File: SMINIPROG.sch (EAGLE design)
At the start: 5 parts

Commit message: Routing for v1.0 release
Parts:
- added J1: ESPROG-SOCKET, SuperHouse-Connectors:ESPROG-SOCKET
- added J2: M01-PLAIN, SuperHouse-Connectors:M01-PLAIN
- added TP6, TP7: POGO-P75-B1, SuperHouse-Test:POGO-P75-B1
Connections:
- new net !RESET: J1.6, TP7.P$1
- new net 3.3V: J1.3, TP1.P$1
- new net GPIO0: J1.2, TP5.P$1
- new net GPIO2: J2.1, TP6.P$1
- new net SONOFF_RX: J1.4, TP4.P$1
- new net SONOFF_TX: J1.5, TP3.P$1
- net GND: now also J1.1
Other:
- note added: "!RESET"
- note added: "GPIO2"
- note removed: "TX and RX connected directly to programmer. Pull 3.3V and GPIO0 low. Raise 3.3V. Hold GPIO0 low for a while, then raise or release."
- moved on the sheet: TP1, TP2, TP3, TP4, TP5

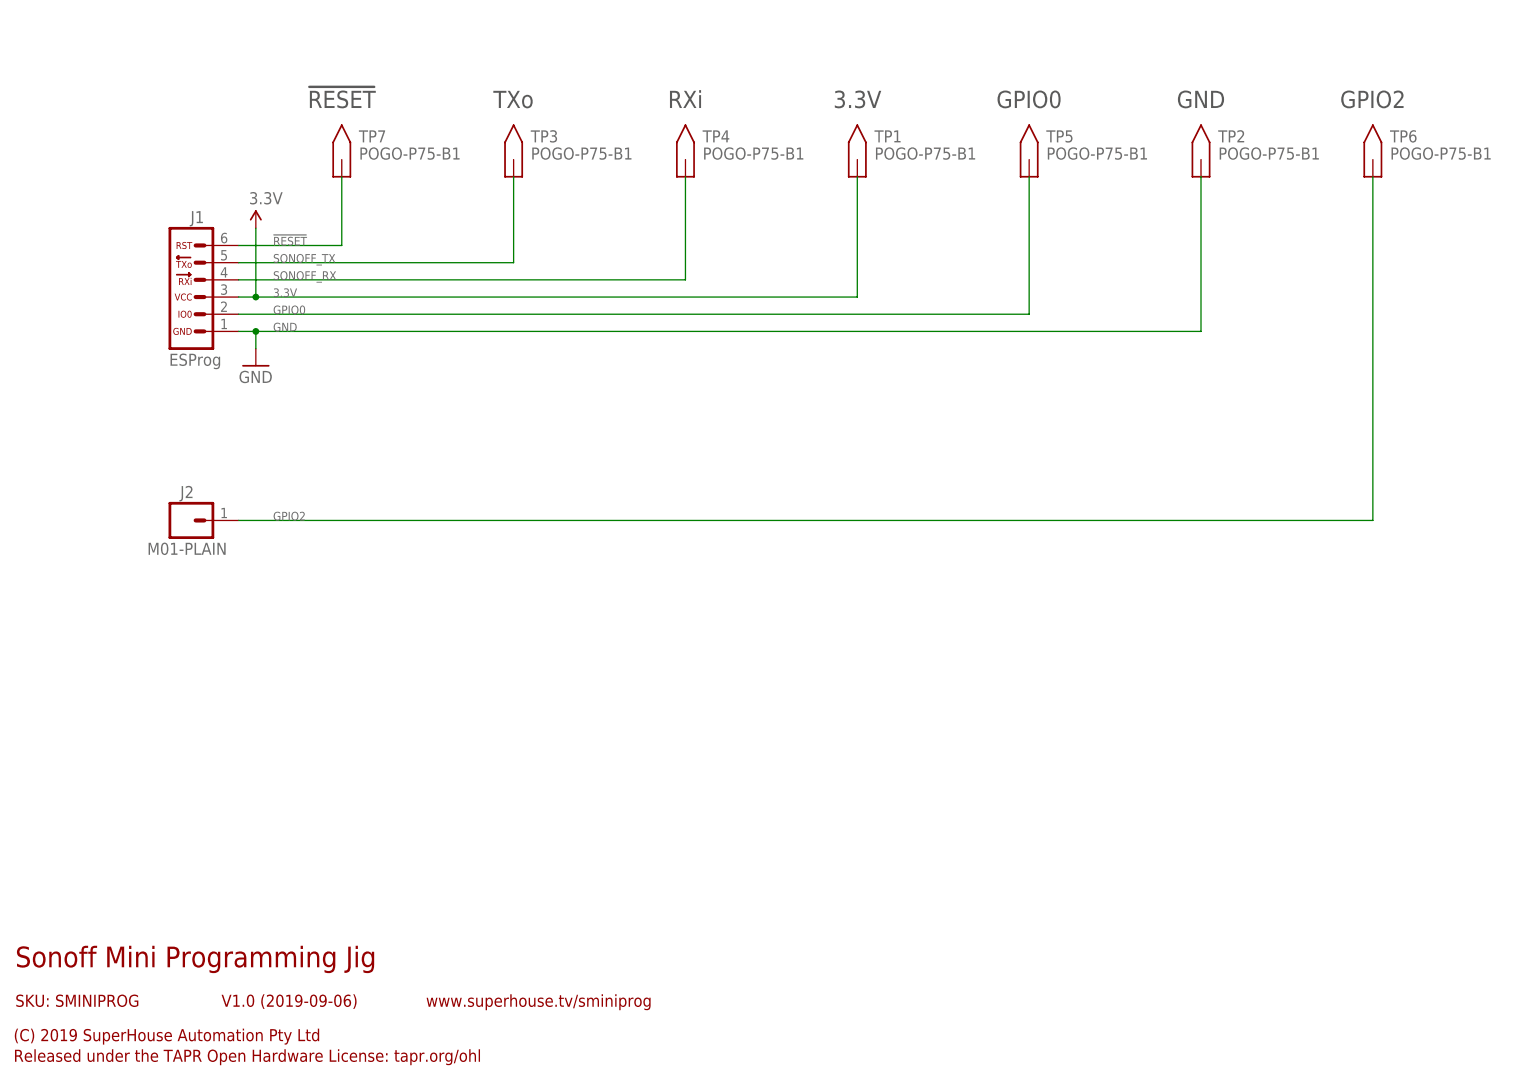
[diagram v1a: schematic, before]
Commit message: Replaced ESP-Prog header, major update for v2.0 release
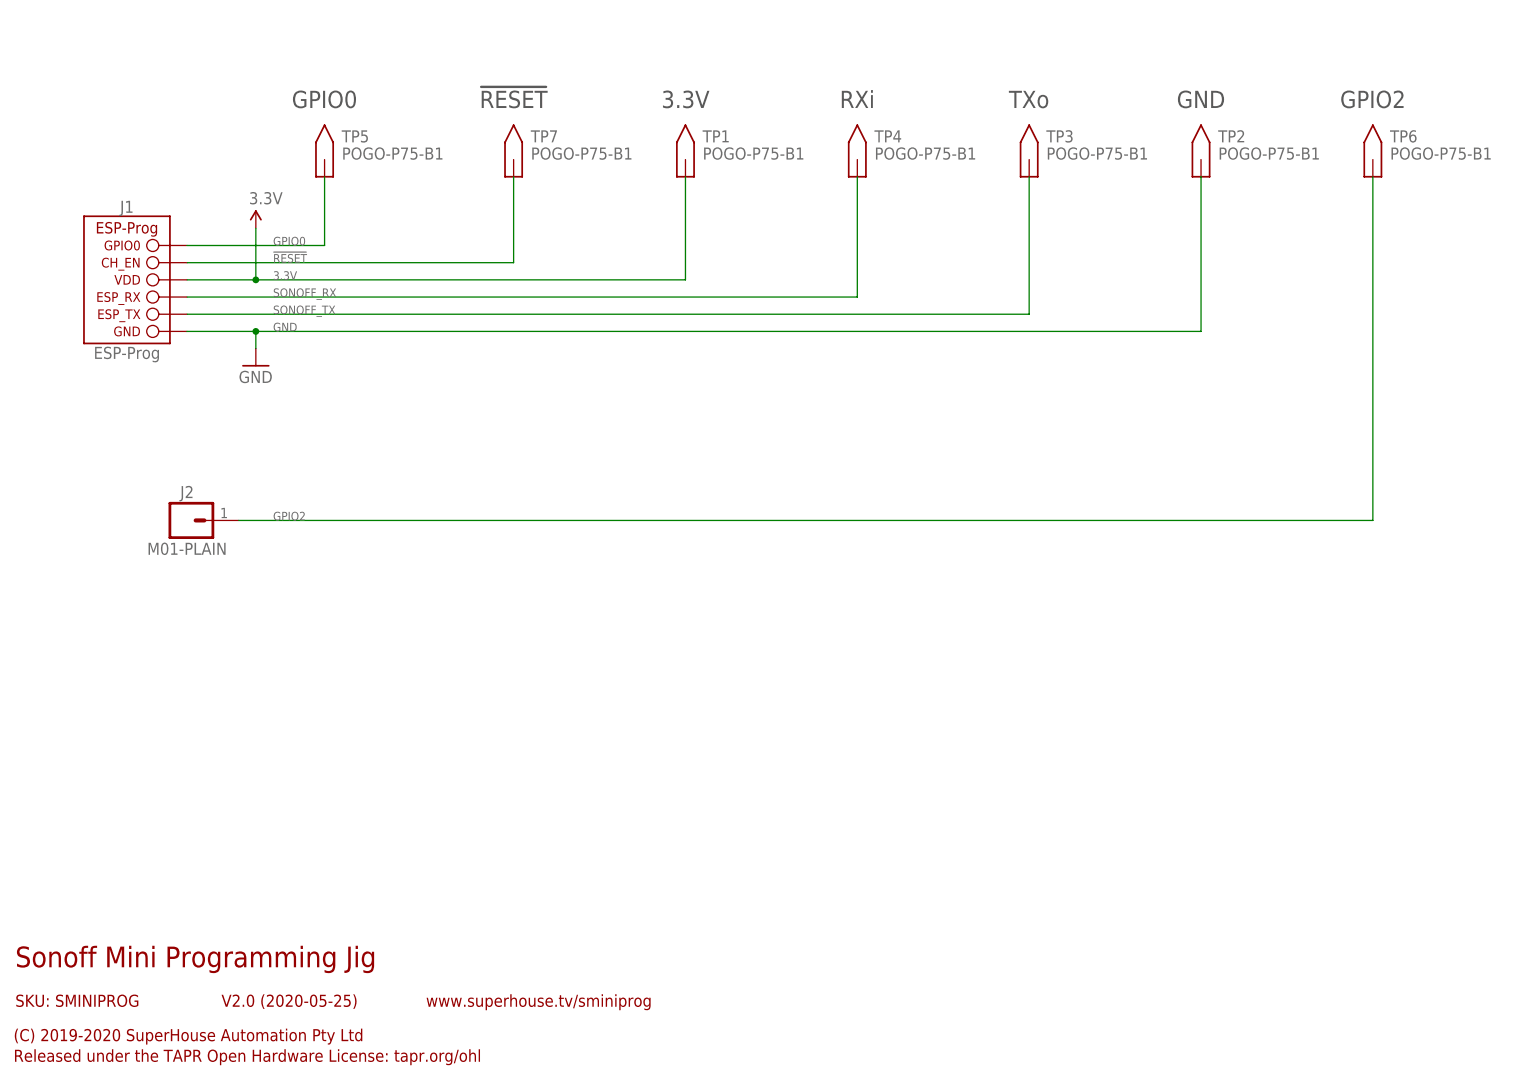
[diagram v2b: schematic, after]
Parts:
- J1: value ESPROG-SOCKET -> ESP-PROG-1X6-2.54-SOCKET-RA; device SuperHouse-Connectors:ESPROG-SOCKET -> SuperHouse-ESP-Prog:ESP-PROG-1X6-2.54-SOCKET-RA
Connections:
- net !RESET: now also J1.CH_EN; no longer J1.6
- net 3.3V: now also J1.VDD; no longer J1.3
- net GND: now also J1.GND; no longer J1.1
- net GPIO0: now also J1.GPIO0; no longer J1.2
- net SONOFF_RX: now also J1.ESP_RX; no longer J1.4
- net SONOFF_TX: now also J1.ESP_TX; no longer J1.5
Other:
- note added: "(C) 2019-2020 SuperHouse Automation Pty Ltd"
- note added: "V2.0 (2020-05-25)"
- note removed: "(C) 2019 SuperHouse Automation Pty Ltd"
- note removed: "V1.0 (2019-09-06)"
- moved on the sheet: TP1, TP3, TP4, TP5, TP7
